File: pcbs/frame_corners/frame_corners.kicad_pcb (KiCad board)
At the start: 2 copper layers, 66 x 40.1 mm, 5 parts, among them J1 Conn_02x20_Odd_Even, J2 Conn_02x08_Odd_Even, J3 Conn_02x08_Odd_Even

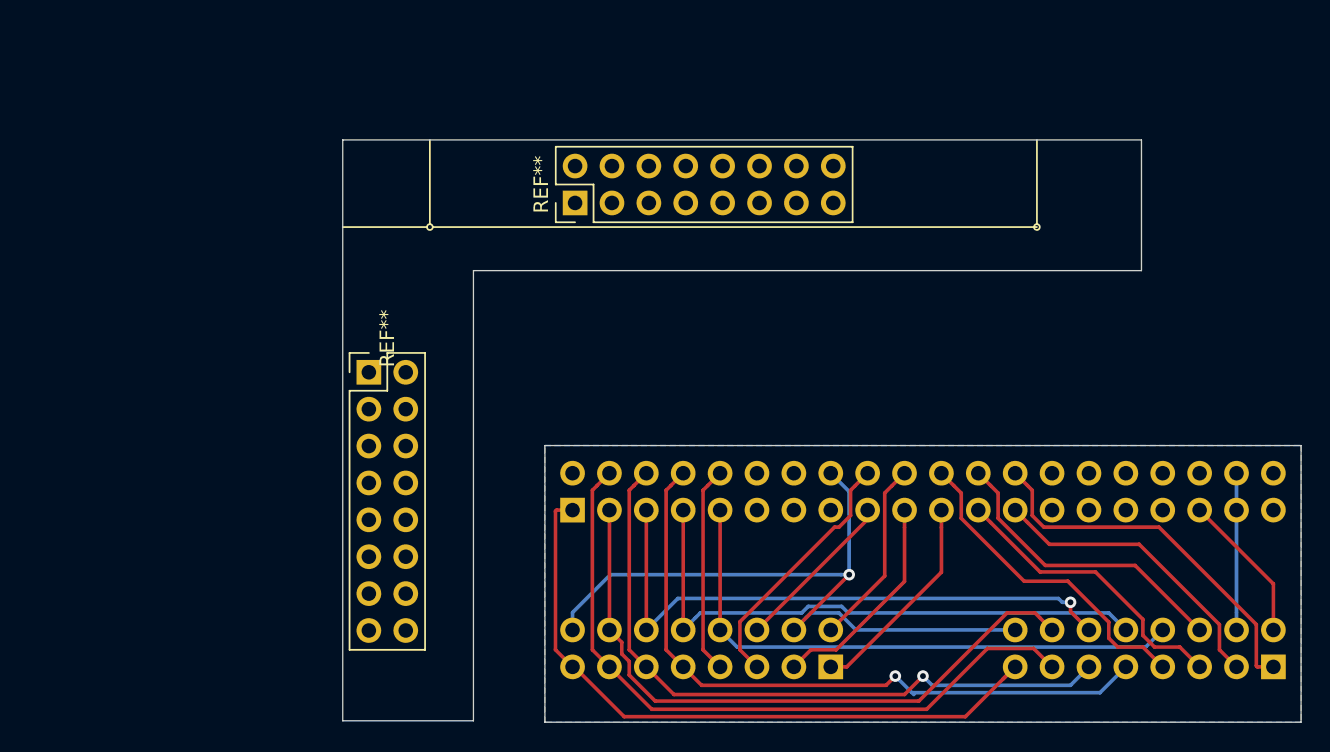
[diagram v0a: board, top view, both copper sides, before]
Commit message: Remove GPIO 2 HUB75 board from frame corners.
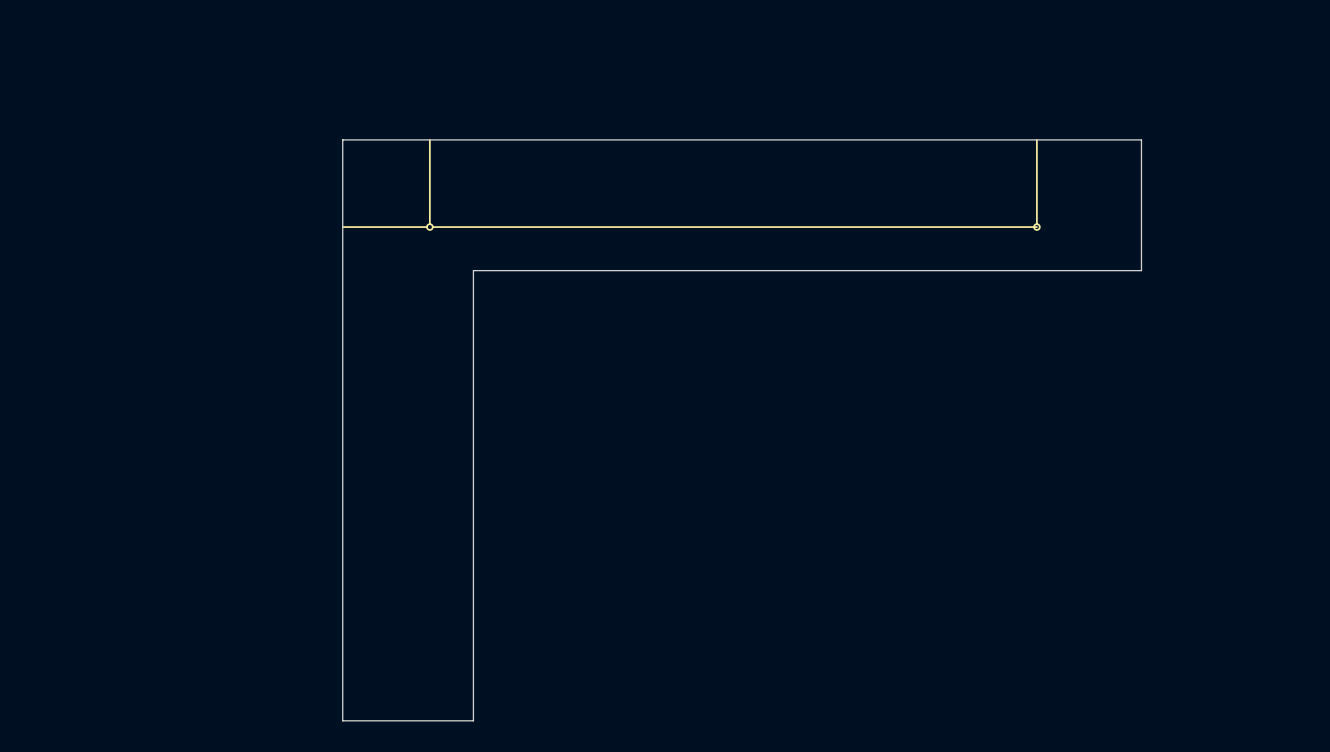
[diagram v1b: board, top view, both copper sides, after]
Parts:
- removed J1: Conn_02x20_Odd_Even, Connector_PinSocket_2.54mm:PinSocket_2x20_P2.54mm_Horizontal
- removed J2, J3: Conn_02x08_Odd_Even, Connector_PinHeader_2.54mm:PinHeader_2x08_P2.54mm_Vertical
- removed REF** (x2): PinHeader_2x08_P2.54mm_Vertical, Connector_PinHeader_2.54mm:PinHeader_2x08_P2.54mm_Vertical
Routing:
- net GND: track 61.2 -> 0.00 mm, vias 1 -> 0
- net /CLK: track 48.3 -> 0.00 mm
- net /OE_: track 46.9 -> 0.00 mm
- net /C: track 46.9 -> 0.00 mm, vias 1 -> 0
- net /A: track 46.8 -> 0.00 mm, vias 1 -> 0
- net /LAT: track 44.8 -> 0.00 mm
- net /D: track 40.9 -> 0.00 mm, vias 1 -> 0
- net /B: track 40.1 -> 0.00 mm
- net /E: track 39.7 -> 0.00 mm
- net /PF0: track 26.0 -> 0.00 mm
- net /B4: track 22.4 -> 0.00 mm
- net /G4: track 20.7 -> 0.00 mm
- net /B3: track 20.7 -> 0.00 mm
- net /PD6: track 20.4 -> 0.00 mm
- net /PD1: track 17.6 -> 0.00 mm
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- removed copper zone on B.Cu, net GND
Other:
- board size 66 x 40.1 mm -> 55 x 40 mm

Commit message: First version
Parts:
- added REF**: MountingHole_2.2mm_M2, MountingHole:MountingHole_2.2mm_M2, F.Cu at (-376.0, -544.0)
- added REF**: PinHeader_2x05_P2.54mm_Vertical, Connector_PinHeader_2.54mm:PinHeader_2x05_P2.54mm_Vertical, F.Cu at (-398.6, -540.0)
- added REF**: PinHeader_2x05_P2.54mm_Vertical, Connector_PinHeader_2.54mm:PinHeader_2x05_P2.54mm_Vertical, B.Cu at (-390.0, -548.6)
- added REF**: MountingHole_2.2mm_M2, MountingHole:MountingHole_2.2mm_M2, F.Cu at (-394.0, -544.0)
- added REF**: PinHeader_2x05_P2.54mm_Vertical, Connector_PinHeader_2.54mm:PinHeader_2x05_P2.54mm_Vertical, B.Cu at (-373.2, -548.6)
- added REF**: PinHeader_2x05_P2.54mm_Vertical, Connector_PinHeader_2.54mm:PinHeader_2x05_P2.54mm_Vertical, F.Cu at (-398.6, -523.2)
- added REF**: MountingHole_2.2mm_M2, MountingHole:MountingHole_2.2mm_M2, F.Cu at (-352.2, -544.0)
- added REF**: MountingHole_2.2mm_M2, MountingHole:MountingHole_2.2mm_M2, F.Cu at (-394.0, -526.0)
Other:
- outline, holes or cut-outs redrawn
